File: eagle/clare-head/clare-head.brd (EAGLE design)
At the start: 51 x 69 mm, 21 parts

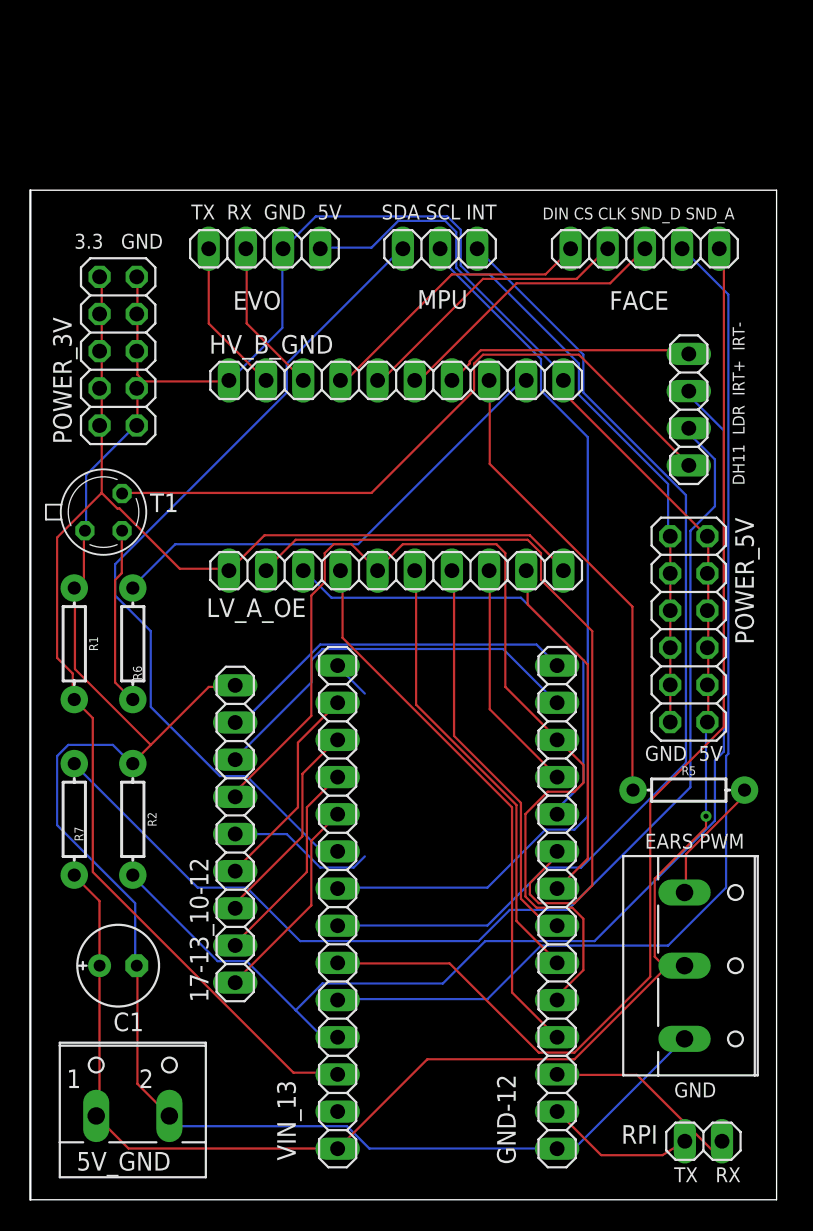
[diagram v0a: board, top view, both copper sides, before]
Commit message: Head pcb v2 submitted for manufacture
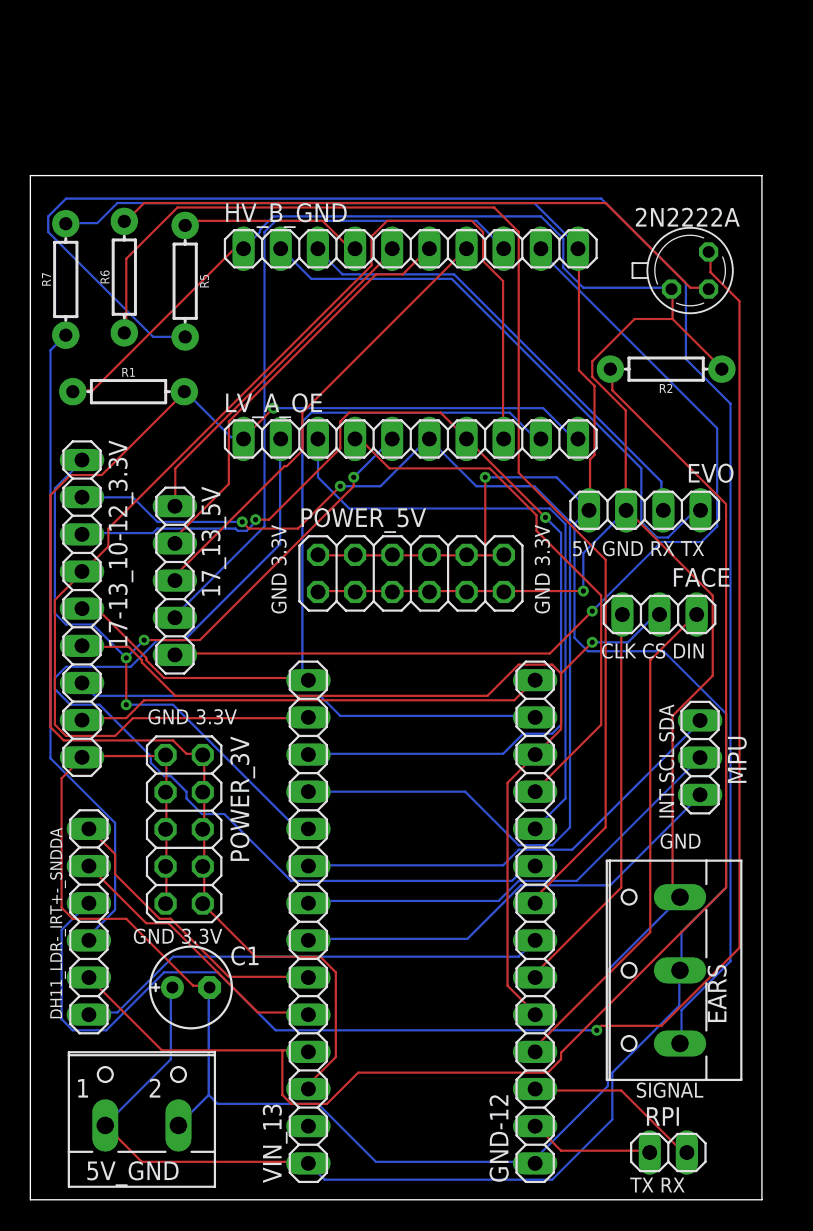
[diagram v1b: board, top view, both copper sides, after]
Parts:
- removed 17-13_10-12: (no value), pinhead:1X09
- removed JP10: (no value), pinhead:1X04
- removed T1: (no value), transistor:TO18
- removed X2: (no value), con-wago-500:W237-103
- added 17-13_10-12_3.3V: (no value), pinhead:1X09
- added 17_13_5V: (no value), pinhead:1X05
- added 2N2222A: (no value), transistor:TO18
- added DH11_LDR-_IRT+-_SNDDA: (no value), pinhead:1X06
- added EARS: (no value), con-wago-500:W237-103
- FACE: device pinhead:1X05 -> pinhead:1X03
- R2: value 1k -> 10k
- R6: value 1.5k -> 2.2k
- R7: value 27 -> 33
- moved R5 48.9 mm to (10.6, 62.8), turned to 270 degrees
- moved R2 47.7 mm to (43.5, 56.8), turned to 180 degrees
- moved MPU 39.1 mm to (45.8, 30.2), turned to 90 degrees
- moved R7 36.9 mm to (2.42, 62.9), turned to 90 degrees
- moved POWER_3V 33.0 mm to (10.5, 25.3), turned to 270 degrees
- moved EVO 31.5 mm to (42.0, 47.1), turned to 180 degrees
- moved R6 25.1 mm to (6.42, 63.1), turned to 90 degrees
- moved FACE 25.0 mm to (43.0, 40.0), turned to 180 degrees
- moved POWER_5V 19.4 mm to (26.0, 42.8), turned to 0 degrees
- moved R1 17.6 mm to (6.71, 55.2), turned to 0 degrees
- moved HV_B_GND 9.06 mm to (26.0, 65.0)
- moved LV_A_OE 9.06 mm to (26.0, 52.0)
- moved C1 5.20 mm to (11.0, 14.5)
- moved RPI 2.52 mm to (43.6, 3.23)
- moved VIN_13 2.24 mm to (19.0, 19.0)
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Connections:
- removed net CLK5: FACE.3, HV_B_GND.6
- removed net CS5: FACE.2, HV_B_GND.5
- removed net DH115: HV_B_GND.7, JP10.1
- removed net DIN5: FACE.1, HV_B_GND.4
- removed net IRT5: HV_B_GND.9, R6.P$1
- removed net LDR: JP10.2, R2.P$2, VIN_13.4
- removed net S$1: VIN_13.14
- new net LDR-: DH11_LDR-_IRT+-_SNDDA.2, R2.P$2, VIN_13.4
- new net N$10: 17_13_5V.5, HV_B_GND.9
- new net N$5: 17_13_5V.1, HV_B_GND.5
- new net N$6: 17_13_5V.2, HV_B_GND.6
- new net N$7: 17_13_5V.3, HV_B_GND.7
- new net N$9: 17_13_5V.4, HV_B_GND.8
- net +5V: now also EARS.2; no longer X2.2
- net CLK: now also FACE.3; no longer LV_A_OE.6
- net CS: now also 17-13_10-12_3.3V.6, FACE.2; no longer 17-13_10-12.6, LV_A_OE.5
- net DH11: now also DH11_LDR-_IRT+-_SNDDA.1; no longer LV_A_OE.7
- net DIN: now also FACE.1; no longer LV_A_OE.4
- net EARS: now also LV_A_OE.4; no longer LV_A_OE.8
- net EARS5: now also EARS.1; no longer X2.1
- net GND: now also 17-13_10-12_3.3V.9, 2N2222A.1, EARS.3; no longer 17-13_10-12.9, T1.1, X2.3
- net IRT: now also R6.P$1; no longer LV_A_OE.9
- net IRT+: now also DH11_LDR-_IRT+-_SNDDA.3; no longer JP10.3
- net IRT-: now also 2N2222A.3, DH11_LDR-_IRT+-_SNDDA.4; no longer JP10.4, T1.3
- net MISO: now also 17-13_10-12_3.3V.8; no longer 17-13_10-12.8
- net MOSI: now also 17-13_10-12_3.3V.7; no longer 17-13_10-12.7
- net N$12: now also 17-13_10-12_3.3V.1, LV_A_OE.5; no longer 17-13_10-12.1
- net N$13: now also 17-13_10-12_3.3V.2, LV_A_OE.6; no longer 17-13_10-12.2
- net N$14: now also 17-13_10-12_3.3V.3, LV_A_OE.7; no longer 17-13_10-12.3
- net N$15: now also 17-13_10-12_3.3V.4, LV_A_OE.8; no longer 17-13_10-12.4
- net N$16: now also 17-13_10-12_3.3V.5, LV_A_OE.9, VIN_13.14; no longer 17-13_10-12.5
- net N$3: now also 2N2222A.2; no longer T1.2
- net N$8: now also HV_B_GND.4; no longer HV_B_GND.8
- net SND_A: now also DH11_LDR-_IRT+-_SNDDA.6; no longer FACE.5
- net SND_D: now also DH11_LDR-_IRT+-_SNDDA.5; no longer FACE.4
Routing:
- net EARS5: track 8.72 -> 114.5 mm
- net LDR-: track 0.00 -> 95.9 mm
- net LDR: track 83.3 -> 0.00 mm
- net N$15: track 14.4 -> 83.6 mm
- net N$13: track 14.4 -> 79.9 mm, vias 0 -> 2
- net N$10: track 0.00 -> 64.8 mm, vias 0 -> 1
- net IRT-: track 46.9 -> 109.5 mm, vias 0 -> 1
- net IRT: track 24.4 -> 84.5 mm
- net SND_A: track 78.0 -> 20.0 mm
- net N$14: track 14.4 -> 72.1 mm, vias 0 -> 2
- net SND_D: track 74.8 -> 19.2 mm
- net +5V: track 134.9 -> 183.6 mm
- net N$12: track 14.4 -> 61.3 mm, vias 0 -> 4
- net N$9: track 0.00 -> 46.4 mm
- net N$16: track 10.1 -> 52.7 mm
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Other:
- board size 51 x 69 mm -> 50 x 70 mm
- board text added: "5V GND RX TX"
- board text added: "CLK CS DIN"
- board text added: "GND 3.3V"
- board text added: "INT SCL SDA"
- board text added: "SIGNAL"
- board text removed: "3.3 GND"
- board text removed: "DH11 LDR IRT+ IRT-"
- board text removed: "DIN CS CLK SND_D SND_A"
- board text removed: "EARS PWM"
- board text removed: "GND 5V"
- board text removed: "SDA SCL INT"
- board text removed: "TX RX GND 5V"

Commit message: 3d pcb version
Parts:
- removed 17-13_10-12_3.3V: (no value), pinhead:1X09
- removed 17_13_5V: (no value), pinhead:1X05
- removed DH11_LDR-_IRT+-_SNDDA: (no value), pinhead:1X06
- removed RPI: (no value), pinhead:1X02
- added 15-13-5V: (no value), pinhead:1X03
- added 15-13_10-12_3V: (no value), pinhead:1X06
- added DH11_LDR+-_IRT+-_SNDDA: (no value), pinhead:1X07
- added RPI-SWPED, SER4: (no value), pinhead:1X02
- FACE, MPU: device pinhead:1X03 -> pinhead:1X05
- POWER_5V: device pinhead:2X06 -> pinhead:2X04
- moved POWER_3V 31.4 mm to (26.3, 52.5), turned to 180 degrees
- moved POWER_5V 19.0 mm to (7.00, 42.0), turned to 270 degrees
- moved MPU 15.8 mm to (47.0, 46.0)
- moved R2 13.9 mm to (36.5, 68.8)
- moved EVO 10.2 mm to (44.0, 57.1)
- moved 2N2222A 10.0 mm to (45.1, 73.5)
- moved R1 10.0 mm to (6.71, 65.2)
- moved R7 10.0 mm to (2.42, 72.9)
- moved HV_B_GND 10.0 mm to (26.0, 75.0)
- moved LV_A_OE 10.0 mm to (26.0, 62.0)
- moved R5 10.0 mm to (10.6, 72.8)
- moved R6 10.0 mm to (6.42, 73.1)
- moved FACE 8.94 mm to (47.0, 32.0), turned to 90 degrees
- moved C1 8.53 mm to (11.5, 23.0), turned to 270 degrees
- moved EARS 1.00 mm to (44.1, 15.7)
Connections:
- removed net N$12: 17-13_10-12_3.3V.1, LV_A_OE.5, VIN_13.10
- removed net N$13: 17-13_10-12_3.3V.2, LV_A_OE.6, VIN_13.11
- removed net N$5: 17_13_5V.1, HV_B_GND.5
- removed net N$6: 17_13_5V.2, HV_B_GND.6
- removed net RXEVO5: EVO.2, HV_B_GND.3
- removed net TXEVO5: EVO.1, HV_B_GND.2
- new net 5V: MPU.5
- new net FCS: FACE.2, GND-12.5
- new net RX4: SER4.2, VIN_13.11
- new net TX4: SER4.1, VIN_13.10
- net +5V: no longer POWER_5V.10, POWER_5V.12
- net 3.3V: now also DH11_LDR+-_IRT+-_SNDDA.2, FACE.5
- net CS: now also 15-13_10-12_3V.4; no longer 17-13_10-12_3.3V.6, FACE.2, GND-12.5
- net DH11: now also DH11_LDR+-_IRT+-_SNDDA.1; no longer DH11_LDR-_IRT+-_SNDDA.1
- net GND: now also FACE.4, MPU.4; no longer 17-13_10-12_3.3V.9, POWER_5V.11, POWER_5V.9
- net IRT+: now also DH11_LDR+-_IRT+-_SNDDA.4; no longer DH11_LDR-_IRT+-_SNDDA.3
- net IRT-: now also DH11_LDR+-_IRT+-_SNDDA.5; no longer DH11_LDR-_IRT+-_SNDDA.4
- net LDR-: now also DH11_LDR+-_IRT+-_SNDDA.3; no longer DH11_LDR-_IRT+-_SNDDA.2
- net MISO: now also 15-13_10-12_3V.6; no longer 17-13_10-12_3.3V.8
- net MOSI: now also 15-13_10-12_3V.5; no longer 17-13_10-12_3.3V.7
- net MPUSCL: now also MPU.3; no longer MPU.2
- net MPUSDA: now also MPU.2; no longer MPU.3
- net N$10: now also 15-13-5V.3; no longer 17_13_5V.5
- net N$14: now also 15-13_10-12_3V.1; no longer 17-13_10-12_3.3V.3
- net N$15: now also 15-13_10-12_3V.2; no longer 17-13_10-12_3.3V.4
- net N$16: now also 15-13_10-12_3V.3; no longer 17-13_10-12_3.3V.5
- net N$7: now also 15-13-5V.1; no longer 17_13_5V.3
- net N$9: now also 15-13-5V.2; no longer 17_13_5V.4
- net RX: now also RPI-SWPED.2; no longer RPI.2
- net RXEVO: now also EVO.2; no longer LV_A_OE.3
- net SND_A: now also DH11_LDR+-_IRT+-_SNDDA.7; no longer DH11_LDR-_IRT+-_SNDDA.6
- net SND_D: now also DH11_LDR+-_IRT+-_SNDDA.6; no longer DH11_LDR-_IRT+-_SNDDA.5
- net TX: now also RPI-SWPED.1; no longer RPI.1
- net TXEVO: now also EVO.1; no longer LV_A_OE.2
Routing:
- net N$13: track 79.9 -> 0.00 mm, vias 2 -> 0
- net N$12: track 61.3 -> 0.00 mm, vias 4 -> 0
- net CS: track 69.4 -> 14.1 mm, vias 1 -> 0
- net N$15: track 83.6 -> 34.6 mm
- net 3.3V: track 99.7 -> 147.1 mm, vias 1 -> 0
- net RX4: track 0.00 -> 42.2 mm
- net TXEVO5: track 39.8 -> 0.00 mm
- net TX4: track 0.00 -> 37.4 mm
- net IRT-: track 109.5 -> 74.0 mm, vias 1 -> 0
- net N$14: track 72.1 -> 39.0 mm, vias 2 -> 0
- net RXEVO5: track 32.1 -> 0.00 mm
- net N$6: track 28.4 -> 0.00 mm
- net +5V: track 183.6 -> 210.7 mm, vias 1 -> 0
- net TXEVO: track 66.4 -> 39.8 mm
- net MISO: track 32.1 -> 6.95 mm
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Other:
- board size 50 x 70 mm -> 50 x 80 mm
- board text added: "3.3V GND"
- board text added: "DIN CS CLK GND 3V"
- board text added: "GND 5V"
- board text added: "INT SDA SCL GND 3V"
- board text removed: "CLK CS DIN"
- board text removed: "GND 3.3V"
- board text removed: "INT SCL SDA"

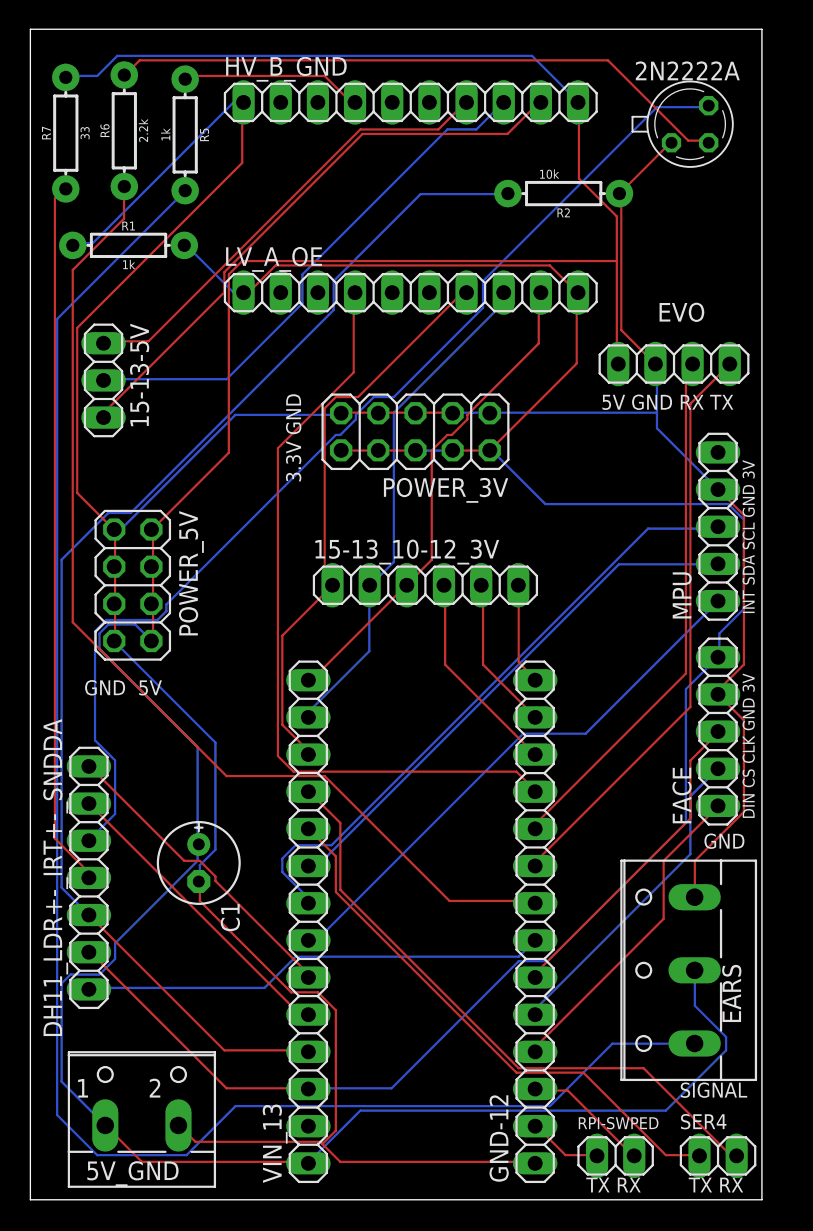
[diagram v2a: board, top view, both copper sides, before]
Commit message: Vcc terminal of the imu was not connected, fixed to connect to 3.3
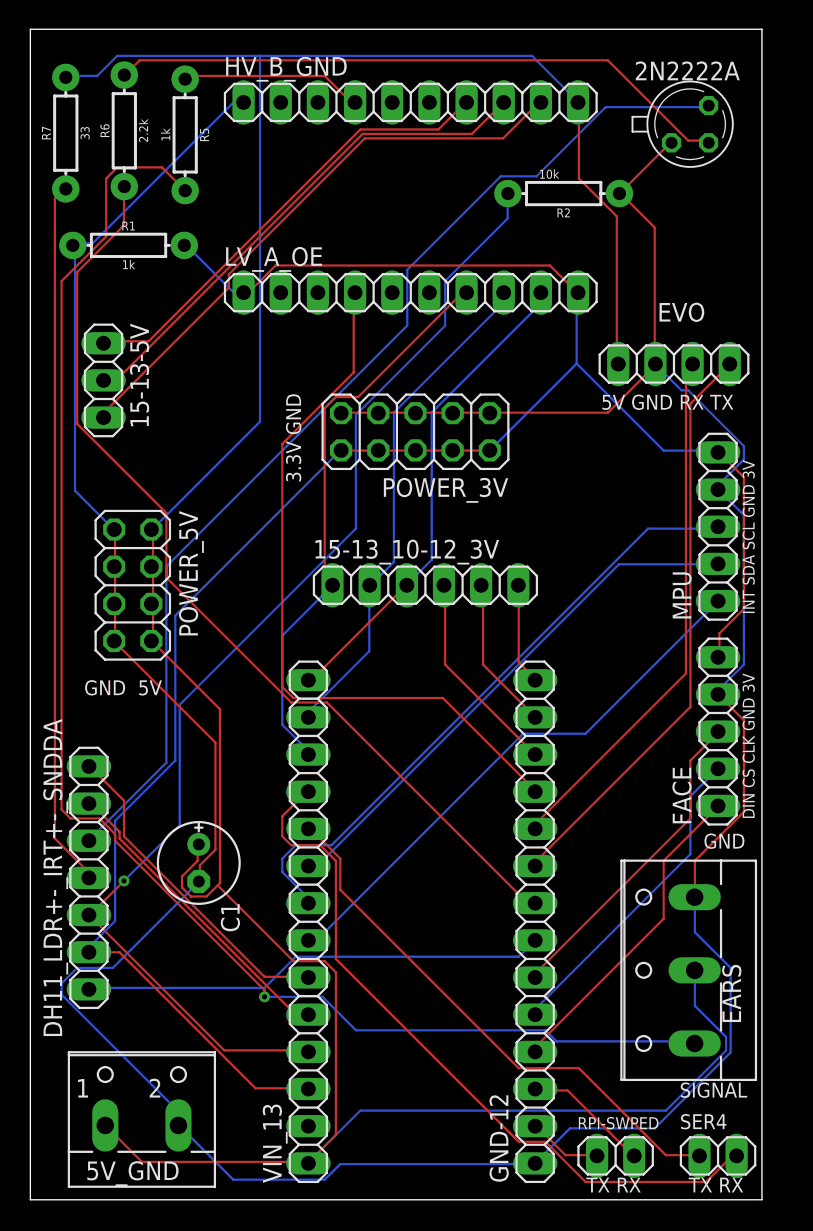
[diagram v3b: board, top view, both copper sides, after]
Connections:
- removed net 5V: MPU.5
- net 3.3V: now also MPU.5
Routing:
- net EARS5: track 114.7 -> 101.2 mm, vias 0 -> 1
- net +5V: track 210.7 -> 202.1 mm
- net RX4: track 42.2 -> 49.3 mm
- net LDR-: track 86.0 -> 80.1 mm, vias 0 -> 1
- net 3.3V: track 147.1 -> 141.2 mm
- net IRT: track 70.8 -> 65.0 mm
- net EARS: track 52.5 -> 49.3 mm
- net N$9: track 36.4 -> 35.2 mm
- net SND_A: track 21.3 -> 22.4 mm
- net GND: track 227.0 -> 228.0 mm
- net IRT-: track 74.0 -> 73.3 mm
